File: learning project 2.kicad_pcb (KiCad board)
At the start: 4 copper layers, 79 x 53 mm, 14 parts, among them U2 MAX30102X, U3 SSD1306

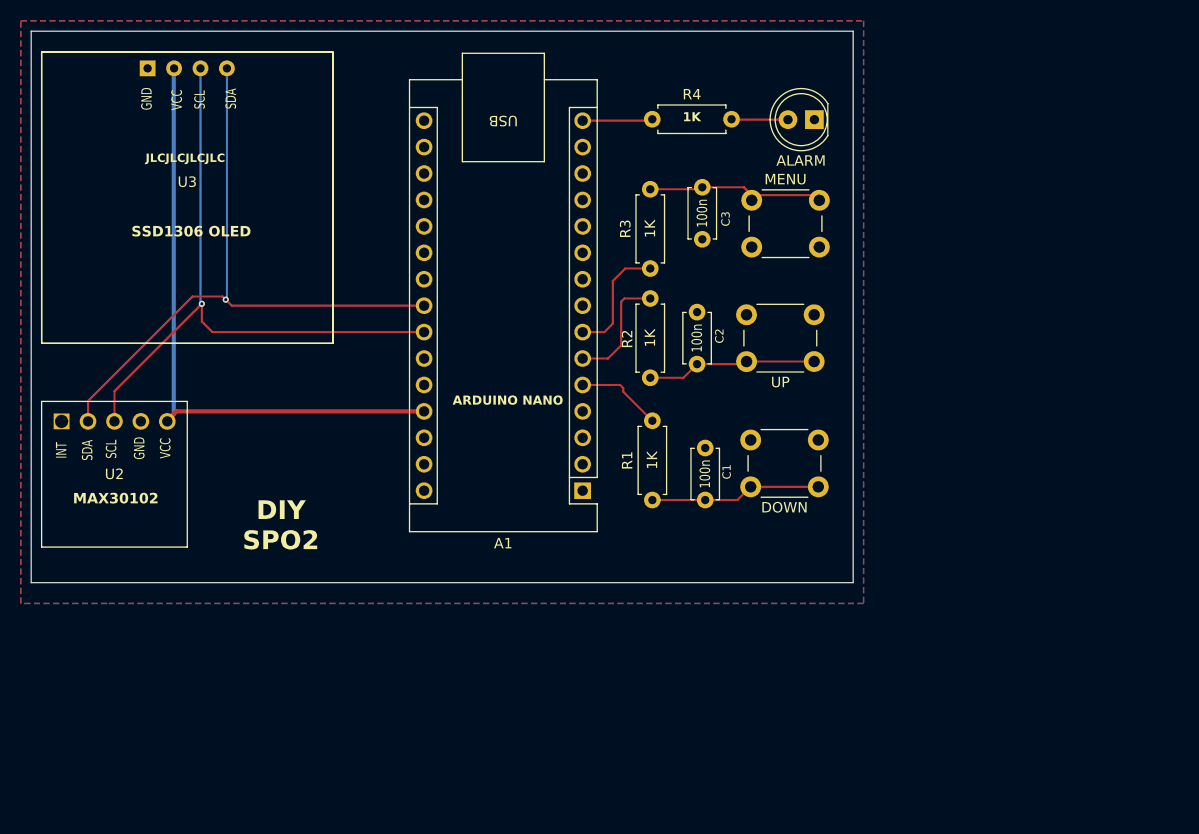
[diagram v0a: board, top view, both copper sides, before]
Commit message: Changed the number of pcb layers from 4 to 2.
Signed-off-by: Naooye <nathanieloyewole@gmail.com>
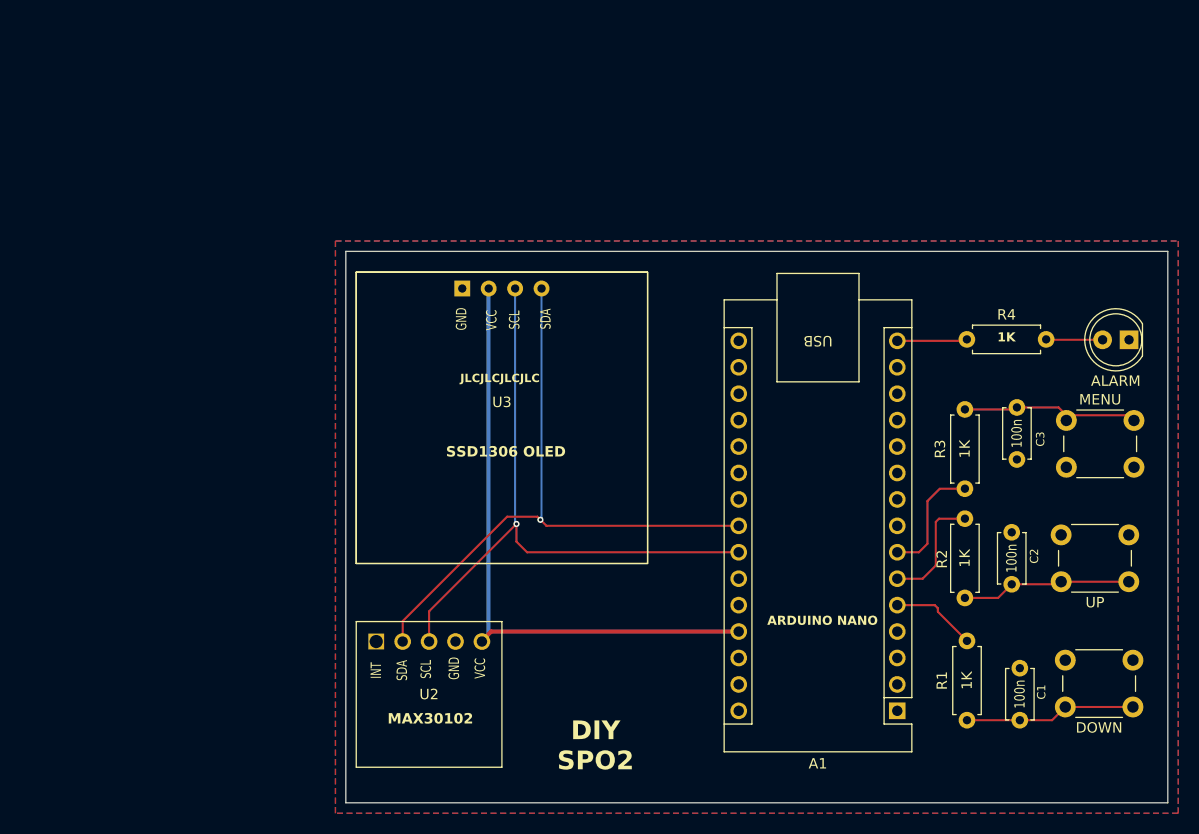
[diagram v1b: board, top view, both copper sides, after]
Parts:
- moved A1 36.9 mm to (163.2, 119.3)
- moved C1 36.9 mm to (175.0, 120.2)
- moved C2 36.9 mm to (174.2, 107.2)
- moved C3 36.9 mm to (174.7, 90.2)
- moved MENU 36.9 mm to (179.5, 91.4)
- moved R1 36.9 mm to (169.9, 112.6)
- moved R2 36.9 mm to (169.7, 100.8)
- moved R3 36.9 mm to (169.7, 98.0)
- moved R4 36.9 mm to (169.9, 83.6)
- moved UP 36.9 mm to (185.5, 106.9)
- moved U2 36.9 mm to (118.2, 117.7)
- moved U3 36.9 mm to (125.2, 90.2)
- moved ALARM 36.9 mm to (185.5, 83.7)
- moved DOWN 36.9 mm to (185.9, 119.0)
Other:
- copper layers 4 -> 2
